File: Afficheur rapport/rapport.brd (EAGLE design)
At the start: 64 x 40 mm, 13 parts, among them IC1 MCP23008P, X1 22-23-2041

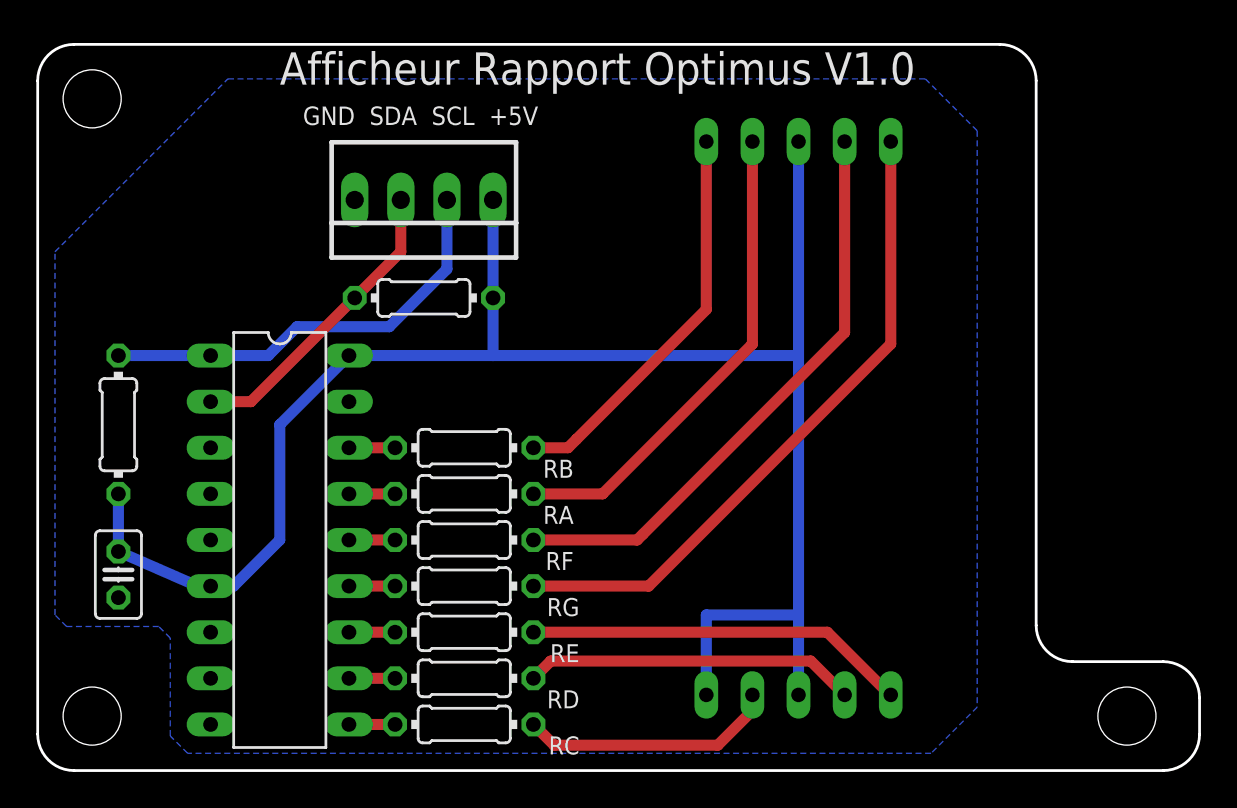
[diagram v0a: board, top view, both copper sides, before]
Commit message: Ajout des modification précédente sur le PCB
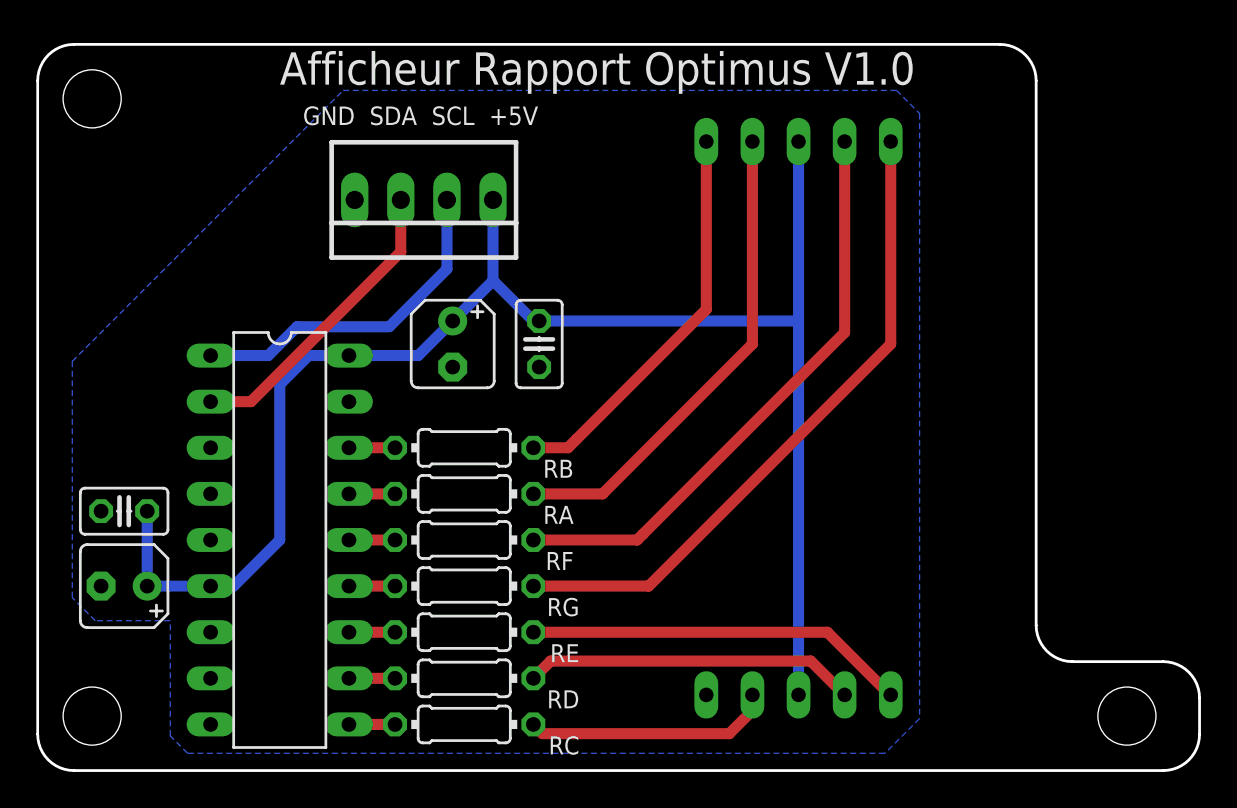
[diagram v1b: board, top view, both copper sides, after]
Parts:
- removed R1, R2: 1k, rcl:0204/7
- added C2: 1µF, resistor:B45181A
- added C3, C4: 27 pF, resistor:C025-025X050
- C1: value 500pF -> 1µF; device rcl:C025-025X050 -> resistor:B45181A
- moved C1 0.71 mm to (4.76, 10.2), turned to 180 degrees
- renumbered X1 to CONN
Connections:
- net +5V: now also C1.+, C2.+, C3.1, C4.1; no longer C1.1, LED1.5, R1.2, R2.1
- net GND: now also C1.-, C2.-, C3.2, C4.2; no longer C1.2
- net SCL: no longer R2.2
- net SDA: no longer R1.1
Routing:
- net +5V: track 98.6 -> 88.7 mm
- net SCL: track 23.9 -> 18.8 mm
- net N$14: track 14.2 -> 13.7 mm

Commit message: Suppression des deux autres condos de lissages pour le Rapport
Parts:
- removed C1, C2: 1µF, resistor:B45181A
- removed C3, C4: 27 pF, resistor:C025-025X050
- added C5: 1µF, resistor:B45181A
- added C6: 27 pF, resistor:C025-025X050
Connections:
- net +5V: now also C5.+, C6.1; no longer C1.+, C2.+, C3.1, C4.1
- net GND: now also C5.-, C6.2; no longer C1.-, C2.-, C3.2, C4.2
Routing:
- net +5V: track 88.7 -> 83.6 mm
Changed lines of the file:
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@@
 <attribute name="SPICEPREFIX" value="R" x="23.495" y="10.16" size="1.778" layer="27" rot="R180" display="off"/>
 </element>
-<element name="C1" library="resistor" library_urn="urn:adsk.eagle:library:348" package="B45181A" package3d_urn="urn:adsk.eagle:package:25796/1" value="1µF" x="4.7625" y="10.16" smashed="yes" rot="R180">
-<attribute name="VALUE" x="8.1915" y="11.2395" size="1.27" layer="27" ratio="10" rot="R270"/>
+<element name="C5" library="resistor" library_urn="urn:adsk.eagle:library:348" package="B45181A" package3d_urn="urn:adsk.eagle:package:25796/1" value="1µF" x="25.7175" y="25.4" smashed="yes">
+<attribute name="VALUE" x="19.558" y="25.019" size="1.27" layer="27" ratio="10"/>
 </element>
-<element name="C2" library="resistor" library_urn="urn:adsk.eagle:library:348" package="B45181A" package3d_urn="urn:adsk.eagle:package:25796/1" value="1µF" x="22.86" y="23.495" smashed="yes" rot="R270">
-<attribute name="VALUE" x="21.1455" y="26.289" size="1.27" layer="27" ratio="10"/>
-</element>
-<element name="C3" library="resistor" library_urn="urn:adsk.eagle:library:348" package="C025-025X050" package3d_urn="urn:adsk.eagle:package:26151/1" value="27 pF" x="27.6225" y="23.495" smashed="yes" rot="R270">
-<attribute name="VALUE" x="24.8285" y="25.781" size="1.27" layer="27" ratio="10" rot="R270"/>
-</element>
-<element name="C4" library="resistor" library_urn="urn:adsk.eagle:library:348" package="C025-025X050" package3d_urn="urn:adsk.eagle:package:26151/1" value="27 pF" x="4.7625" y="14.2875" smashed="yes" rot="R180">
-<attribute name="VALUE" x="7.0485" y="17.0815" size="1.27" layer="27" ratio="10" rot="R180"/>
+<element name="C6" library="resistor" library_urn="urn:adsk.eagle:library:348" package="C025-025X050" package3d_urn="urn:adsk.eagle:package:26151/1" value="27 pF" x="25.7175" y="21.59" smashed="yes">
+<attribute name="VALUE" x="18.669" y="20.701" size="1.27" layer="27" ratio="10"/>
 </element>
 </elements>
@@
 <contactref element="CONN" pad="4"/>
 <polygon width="0.1524" layer="16">
-<vertex x="3.175" y="8.255"/>
-<vertex x="1.905" y="9.525"/>
-<vertex x="1.905" y="22.5425"/>
-<vertex x="16.8275" y="37.465"/>
-<vertex x="47.3075" y="37.465"/>
-<vertex x="48.5775" y="36.195"/>
+<vertex x="7.3025" y="28.2575"/>
+<vertex x="15.875" y="36.83"/>
+<vertex x="47.3075" y="36.83"/>
+<vertex x="48.5775" y="35.56"/>
 <vertex x="48.5775" y="2.8575"/>
 <vertex x="46.6725" y="0.9525"/>
 <vertex x="8.255" y="0.9525"/>
 <vertex x="7.3025" y="1.905"/>
-<vertex x="7.3025" y="8.255"/>
 </polygon>
-<contactref element="C1" pad="-"/>
-<contactref element="C2" pad="-"/>
-<contactref element="C4" pad="2"/>
-<contactref element="C3" pad="2"/>
+<contactref element="C5" pad="-"/>
+<contactref element="C6" pad="2"/>
 </signal>
 <signal name="+5V">
 <contactref element="IC1" pad="6"/>
 <contactref element="CONN" pad="1"/>
-<wire x1="8.799284375" y1="10.16" x2="9.525" y2="10.16" width="0.6096" layer="16"/>
-<wire x1="9.525" y1="10.16" x2="10.795" y2="10.16" width="0.6096" layer="16"/>
-<wire x1="13.335" y1="12.7" x2="10.795" y2="10.16" width="0.6096" layer="16"/>
+<wire x1="13.335" y1="13.97" x2="9.525" y2="10.16" width="0.6096" layer="16"/>
 <contactref element="LED1" pad="8"/>
 <contactref element="LED1" pad="3"/>
 <contactref element="IC1" pad="18"/>
-<contactref element="C2" pad="+"/>
-<contactref element="C1" pad="+"/>
-<wire x1="41.91" y1="34.6475" x2="41.91" y2="24.765" width="0.6096" layer="16"/>
-<wire x1="41.91" y1="24.765" x2="41.91" y2="4.1675" width="0.6096" layer="16"/>
-<wire x1="17.145" y1="22.86" x2="17.24025" y2="22.95525" width="0.6096" layer="16"/>
-<wire x1="25.0825" y1="31.4325" x2="25.0825" y2="26.9875" width="0.6096" layer="16"/>
-<wire x1="25.0825" y1="26.9875" x2="22.86" y2="24.765" width="0.6096" layer="16"/>
-<wire x1="22.86" y1="24.765" x2="20.955" y2="22.86" width="0.6096" layer="16"/>
-<wire x1="20.955" y1="22.86" x2="17.145" y2="22.86" width="0.6096" layer="16"/>
-<wire x1="17.145" y1="22.86" x2="14.9225" y2="22.86" width="0.6096" layer="16"/>
-<wire x1="14.9225" y1="22.86" x2="13.335" y2="21.2725" width="0.6096" layer="16"/>
-<wire x1="13.335" y1="21.2725" x2="13.335" y2="12.7" width="0.6096" layer="16"/>
-<wire x1="9.525" y1="10.16" x2="6.0325" y2="10.16" width="0.6096" layer="16"/>
-<contactref element="C4" pad="1"/>
-<contactref element="C3" pad="1"/>
-<wire x1="25.0825" y1="26.9875" x2="27.305" y2="24.765" width="0.6096" layer="16"/>
-<wire x1="27.305" y1="24.765" x2="27.6225" y2="24.765" width="0.6096" layer="16"/>
-<wire x1="27.6225" y1="24.765" x2="41.91" y2="24.765" width="0.6096" layer="16"/>
-<wire x1="6.0325" y1="10.16" x2="6.0325" y2="14.2875" width="0.6096" layer="16"/>
+<wire x1="41.91" y1="34.6475" x2="41.91" y2="19.3675" width="0.6096" layer="16"/>
+<wire x1="41.91" y1="19.3675" x2="41.91" y2="4.1675" width="0.6096" layer="16"/>
+<wire x1="17.145" y1="22.86" x2="15.5575" y2="22.86" width="0.6096" layer="16"/>
+<wire x1="15.5575" y1="22.86" x2="13.335" y2="20.6375" width="0.6096" layer="16"/>
+<wire x1="13.335" y1="20.6375" x2="13.335" y2="13.97" width="0.6096" layer="16"/>
+<contactref element="C5" pad="+"/>
+<contactref element="C6" pad="1"/>
+<wire x1="25.0825" y1="31.4325" x2="25.0825" y2="26.035" width="0.6096" layer="16"/>
+<wire x1="25.0825" y1="26.035" x2="24.4475" y2="25.4" width="0.6096" layer="16"/>
+<wire x1="24.4475" y1="25.4" x2="24.4475" y2="21.59" width="0.6096" layer="16"/>
+<wire x1="24.4475" y1="21.59" x2="18.415" y2="21.59" width="0.6096" layer="16"/>
+<wire x1="18.415" y1="21.59" x2="17.145" y2="22.86" width="0.6096" layer="16"/>
+<wire x1="24.4475" y1="21.59" x2="26.67" y2="19.3675" width="0.6096" layer="16"/>
+<wire x1="26.67" y1="19.3675" x2="41.91" y2="19.3675" width="0.6096" layer="16"/>
 </signal>
 <signal name="SCL">
